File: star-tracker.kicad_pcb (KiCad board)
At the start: 2 copper layers, 92 x 50 mm, 40 parts, among them J1 Battery, J2 UART, J3 I/O Breakout, J4 JTAG, J5 Stepper Motor, SW1 Power Switch, U1 ESP32-WROOM-32, U2 PTN78000W_EUS-5, U3 A4988

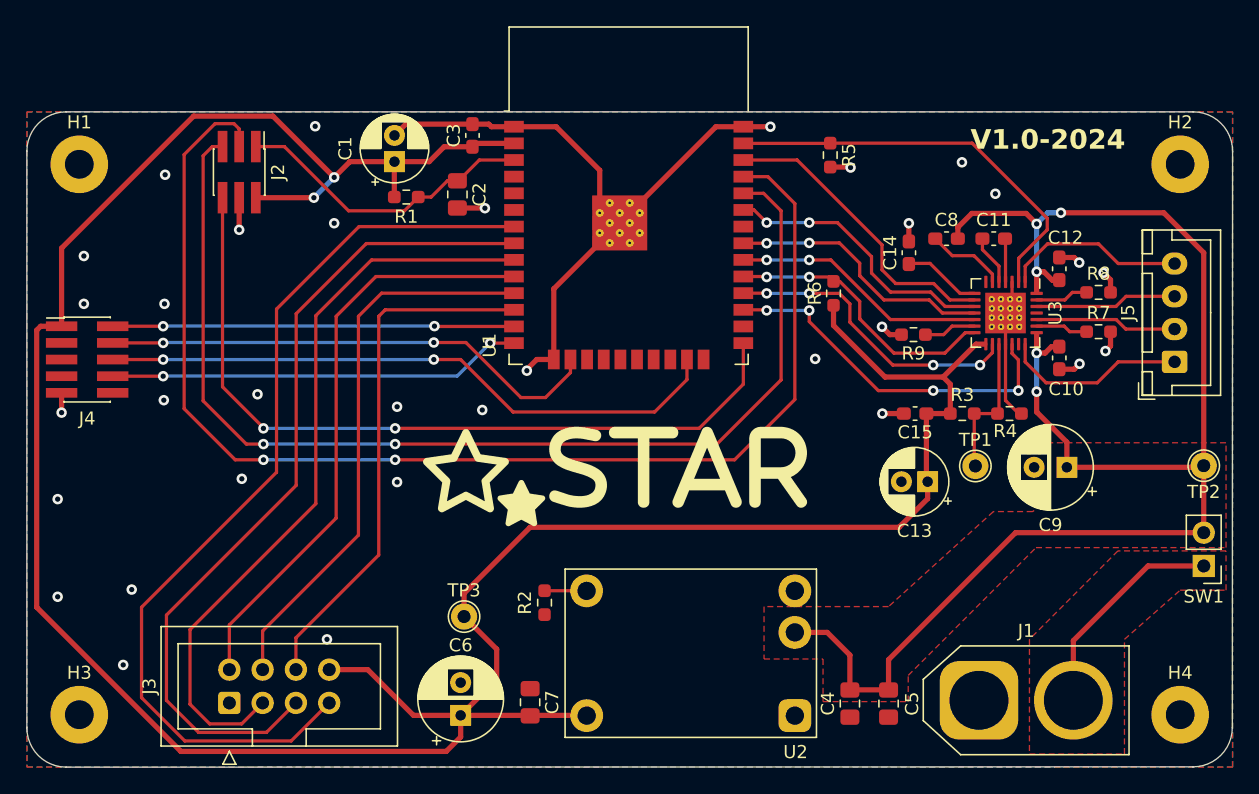
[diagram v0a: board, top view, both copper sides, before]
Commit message: updated track widths, teardrops
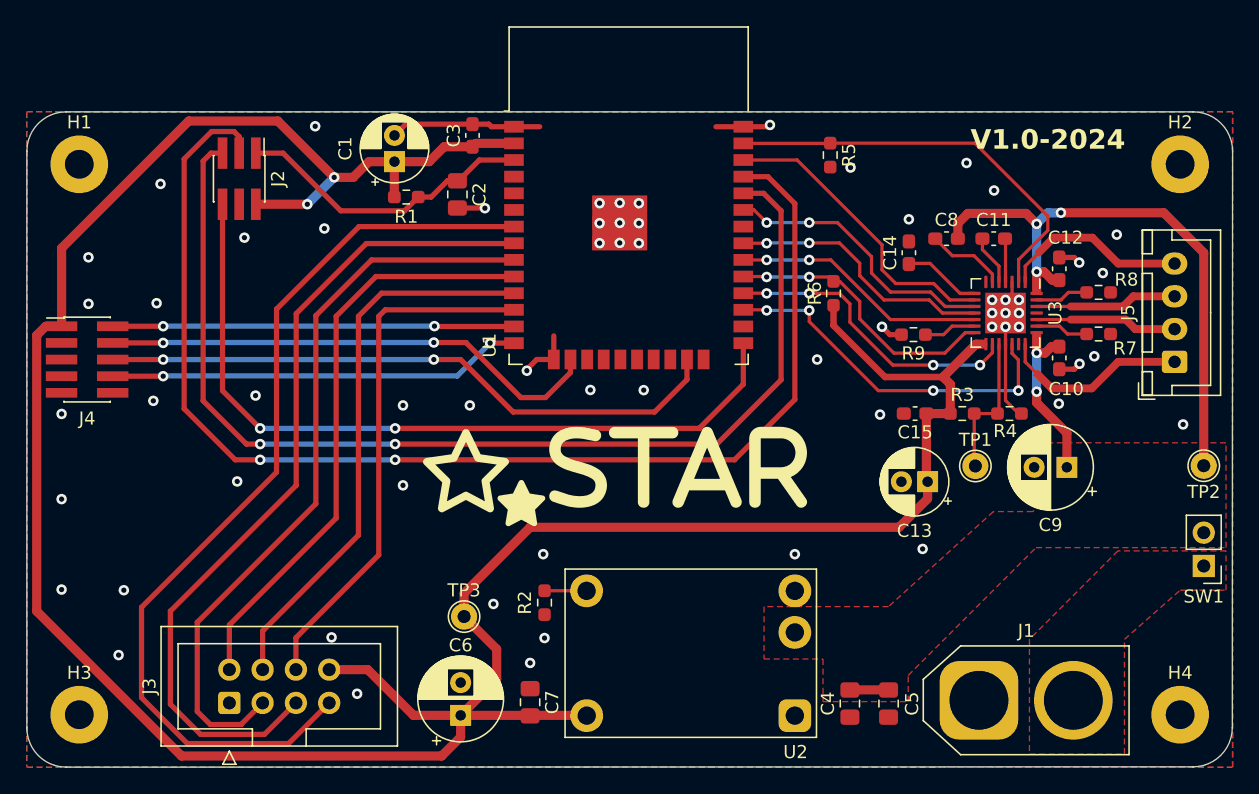
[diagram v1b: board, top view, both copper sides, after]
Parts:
- U1: value ESP32-WROOM-32 -> ESP32-WROOM-32-No-Thermal-Vias; footprint RF_Module:ESP32-WROOM-32 -> custom:ESP32-WROOM-32-No-Thermal-Vias
- U3: footprint Package_DFN_QFN:QFN-28-1EP_5x5mm_P0.5mm_EP3.1x3.1mm_ThermalVias -> Package_DFN_QFN:QFN-28-1EP_5x5mm_P0.5mm_EP3.1x3.1mm
- moved J2 0.50 mm to (54.2, 70.1)
- moved R7 0.17 mm to (119.8, 82.0)
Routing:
- net +12V: track 115.1 -> 61.6 mm
- net GND: track 75.2 -> 37.1 mm, vias 33 -> 63
- net VBAT: track 16.9 -> 0.00 mm
- net /TXD0: track 95.9 -> 95.4 mm

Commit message: changed esp32 footprint
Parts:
- U1: value ESP32-WROOM-32-No-Thermal-Vias -> ESP32-WROOM-32D-No-Thermal-Vias; footprint custom:ESP32-WROOM-32-No-Thermal-Vias -> custom:ESP32-WROOM-32D-No-Thermal-Vias
- moved C1 0.20 mm to (66.0, 69.0)
- moved R1 0.20 mm to (67.0, 71.7)

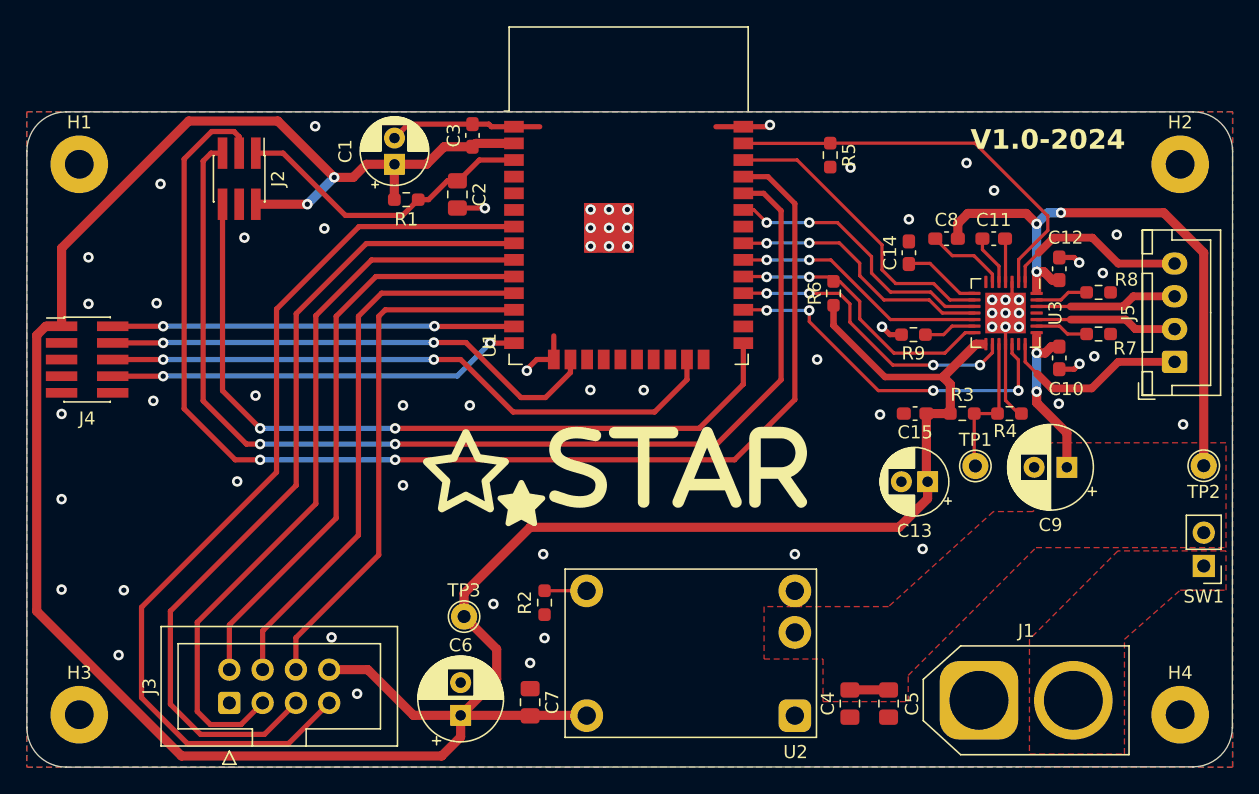
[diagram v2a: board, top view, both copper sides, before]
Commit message: some tweaks, footprint change
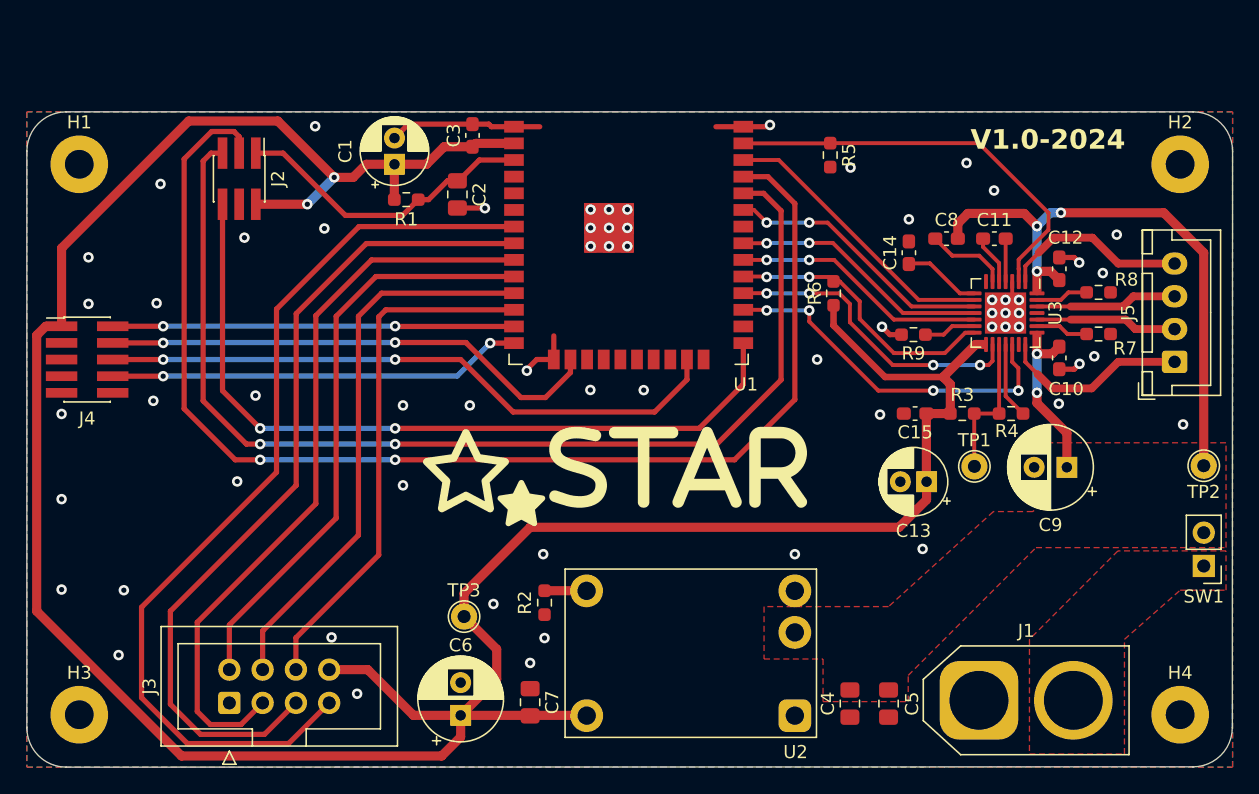
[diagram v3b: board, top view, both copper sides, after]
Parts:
- U3: footprint Package_DFN_QFN:QFN-28-1EP_5x5mm_P0.5mm_EP3.1x3.1mm -> custom:QFN-28-1EP_5x5mm_P0.5mm_EP3.1x3.1mm_Extended Pins
- moved R4 0.12 mm to (113.1, 88.0)
- moved TP1 0.08 mm to (110.3, 92.0)
- moved C13 0.08 mm to (106.7, 93.2)
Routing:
- net +12V: track 61.6 -> 58.6 mm
- net /MS1: track 23.2 -> 22.1 mm
- net /MS2: track 21.4 -> 20.7 mm
- net /MS3: track 20.4 -> 19.9 mm
